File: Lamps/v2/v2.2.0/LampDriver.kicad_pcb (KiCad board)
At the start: 2 copper layers, 50 x 42.8 mm, 25 parts, among them J1 JST XH 1x4, J2 Screw_Terminal_01x02, J3 1x6 MOLEX KK 396, Q1 BSS138, Q2 BSS138, Q3 BSS138, Q4 FDD4141, Q5 FDD4141, Q6 FDD4141

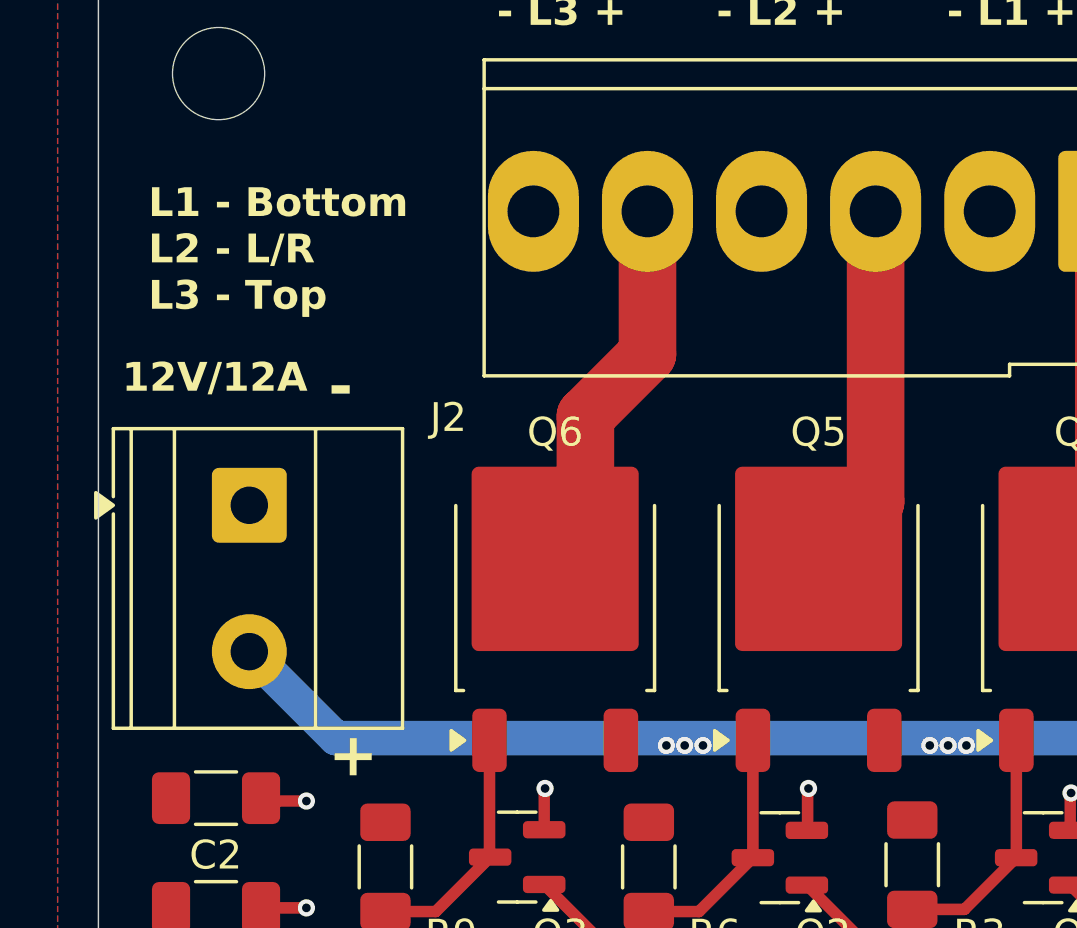
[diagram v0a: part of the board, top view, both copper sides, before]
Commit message: Lamps: PCB: Last touches
Signed-off-by: Patrick Pedersen <ctx.xda@gmail.com>
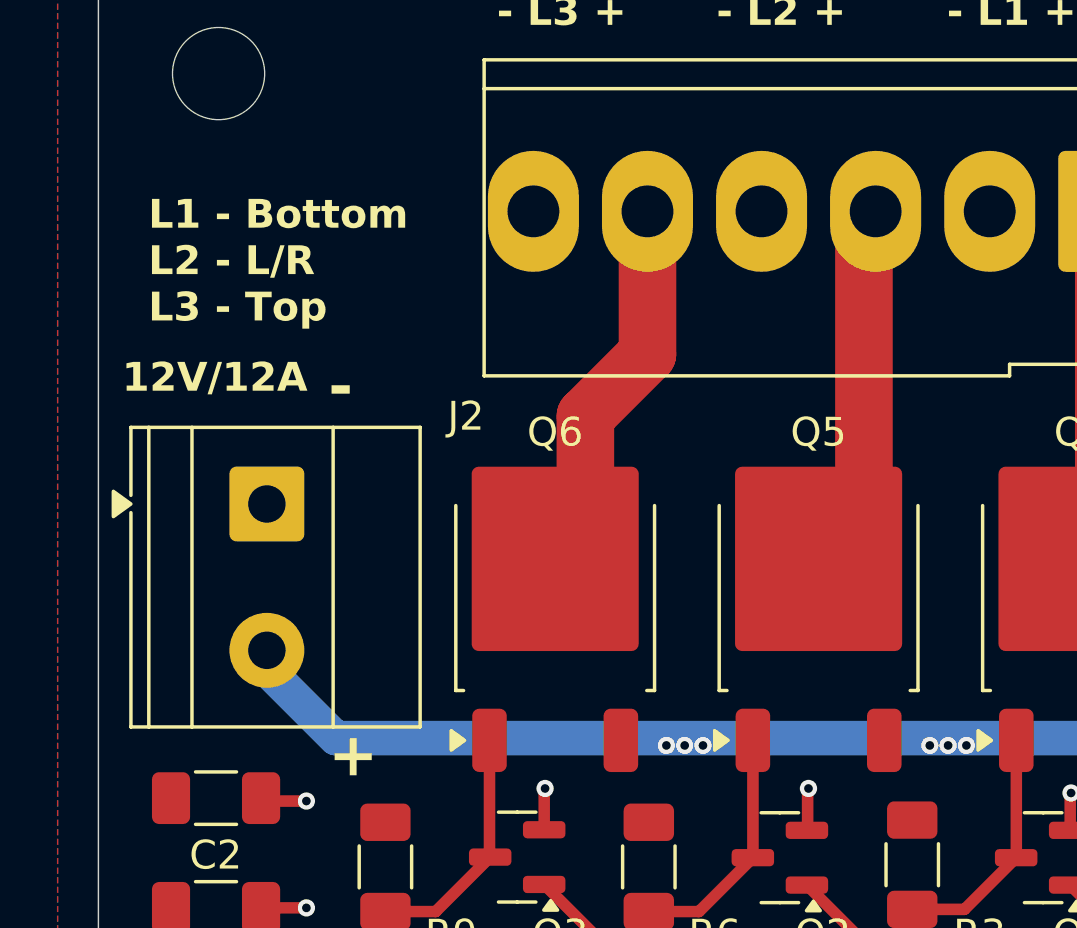
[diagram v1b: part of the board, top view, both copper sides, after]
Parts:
- moved J2 0.61 mm to (87.3, 57.7)
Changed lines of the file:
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@@
 			(outputformat 1)
 			(mirror no)
-			(drillshape 1)
+			(drillshape 0)
 			(scaleselection 1)
-			(outputdirectory "")
+			(outputdirectory "Gerbers/")
 		)
 	)
@@
 	(footprint "TerminalBlock_Phoenix:TerminalBlock_Phoenix_MKDS-1,5-2-5.08_1x02_P5.08mm_Horizontal"
 		(layer "F.Cu")
-		(at 86.6648 57.7038 -90)
+		(at 87.2744 57.658 -90)
 		(descr "Terminal Block Phoenix MKDS-1,5-2-5.08, 2 pins, pitch 5.08mm, size 10.2x9.8mm, drill diameter 1.3mm, pad diameter 2.6mm, http://www.farnell.com/datasheets/100425.pdf, script-generated using https://gitlab.com/kicad/libraries/kicad-footprint-generator/-/tree/master/scripts/TerminalBlock_Phoenix")
 		(tags "THT Terminal Block Phoenix MKDS-1,5-2-5.08 pitch 5.08mm size 10.2x9.8mm drill 1.3mm pad 2.6mm")
@@
 	)
 	(gr_text "L1 - Bottom\nL2 - L/R\nL3 - Top"
-		(at 83.1596 51.0032 0)
+		(at 83.1596 51.4096 0)
 		(layer "F.SilkS")
 		(effects
@@
 	)
 	(segment
-		(start 108.406 57.583)
-		(end 106.426 59.563)
+		(start 108 47.906)
+		(end 108 57.989)
 		(width 2)
 		(layer "F.Cu")
@@
 	(segment
 		(start 108.406 47.5)
-		(end 108.406 57.583)
+		(end 108 47.906)
+		(width 2)
+		(layer "F.Cu")
+		(net 3)
+	)
+	(segment
+		(start 108 57.989)
+		(end 106.426 59.563)
 		(width 2)
 		(layer "F.Cu")
@@
 	)
 	(segment
-		(start 119.7356 65.786)
-		(end 89.667 65.786)
+		(start 87.2744 63.3934)
+		(end 87.2744 62.738)
 		(width 1.2)
 		(layer "B.Cu")
@@
 	(segment
 		(start 89.667 65.786)
-		(end 86.6648 62.7838)
+		(end 87.2744 63.3934)
+		(width 1.2)
+		(layer "B.Cu")
+		(net 8)
+	)
+	(segment
+		(start 119.7356 65.786)
+		(end 89.667 65.786)
 		(width 1.2)
 		(layer "B.Cu")
